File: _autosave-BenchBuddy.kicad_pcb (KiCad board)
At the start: 4 copper layers, 165.1 x 63.5 mm, 133 parts, among them K1 1461069-5, P1 24 Pin MiniFit JR, P2 CONN_3X2, P3 CONN_2, P4 12 Pin Terminal Block, P5 3 Pin TB, Q1 2N3904, Q2 DMN65D8L-7, Q3 AOD476, Q4 AOD476, SW1 Power Switch, U1 LTV-816S, U11 LM317, U2 MCP3901, U3 LMT84, U4 OPA4170, U5 MCP4801, U6 LM337T, U7 AP5726, U8 LM337T, U9 LM317

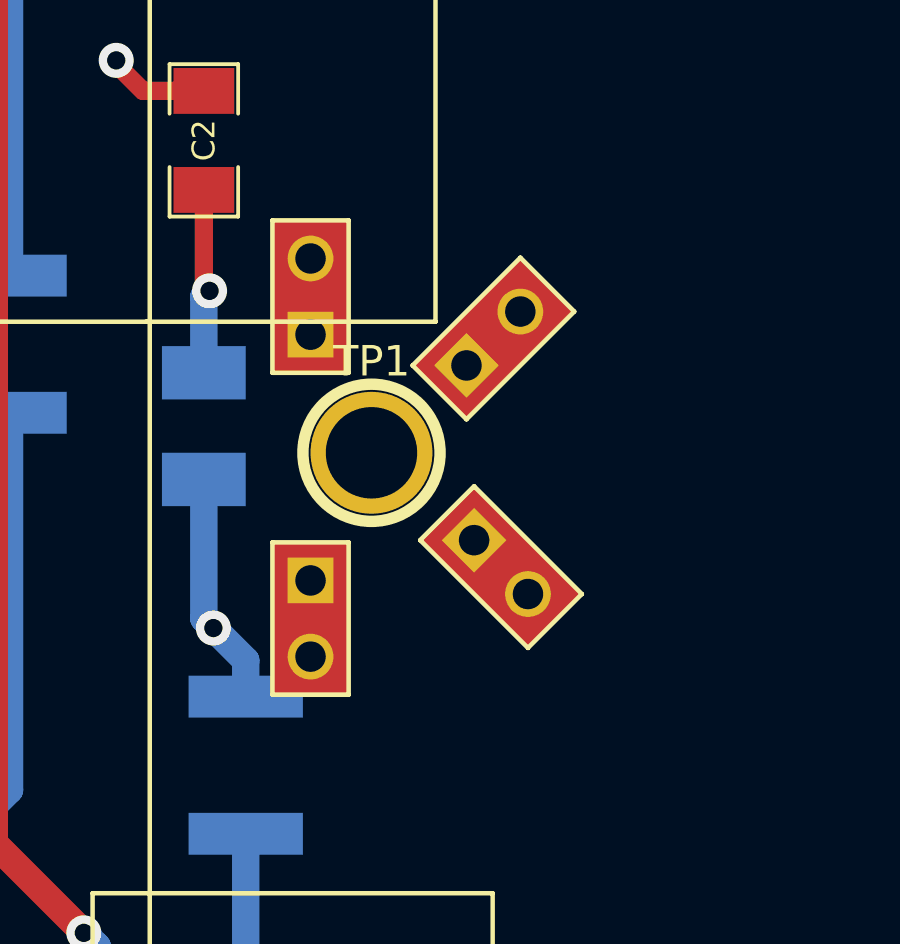
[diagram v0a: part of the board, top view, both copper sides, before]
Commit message: Connecting Grounds Together
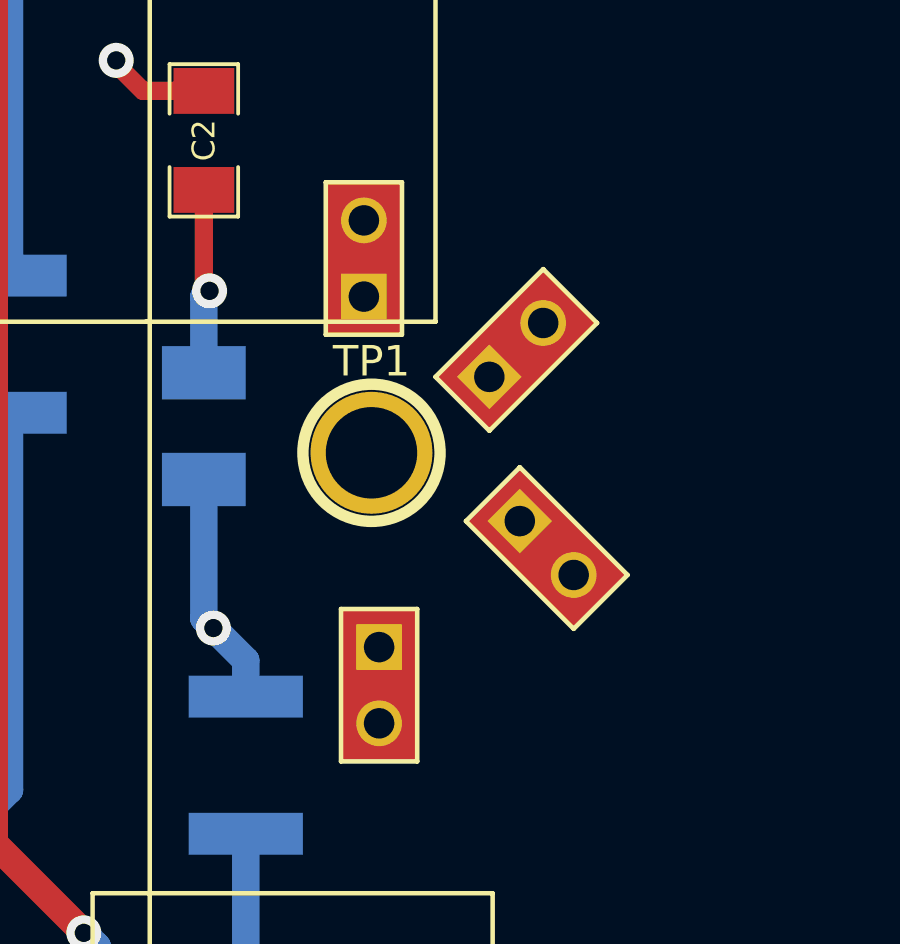
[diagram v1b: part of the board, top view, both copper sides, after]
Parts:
- moved JP4 3.19 mm to (89.9, 121.4)
- moved JP2 2.18 mm to (89.4, 107.2)
- moved JP3 1.65 mm to (95.5, 116.8)
- moved JP1 0.85 mm to (94.5, 110.2)
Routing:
- net GND: track 30.6 -> 33.9 mm
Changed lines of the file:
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@@
   (general
     (links 335)
-    (no_connects 288)
+    (no_connects 287)
     (area 45.180556 57.588999 238.38044 142.307)
     (thickness 1.6)
     (drawings 5)
-    (tracks 129)
+    (tracks 131)
     (zones 0)
     (modules 133)
@@
   )
   (module GND_POINT (layer F.Cu)
-    (at 87.63 119.1895 270)
+    (at 89.916 121.412 270)
     (descr "Connecteurs 2 pins")
     (tags "CONN DEV")
@@
   )
   (module GND_POINT (layer F.Cu)
-    (at 93.98 117.475 315)
+    (at 95.504 116.84 315)
     (descr "Connecteurs 2 pins")
     (tags "CONN DEV")
@@
   )
   (module GND_POINT (layer F.Cu)
-    (at 87.63 108.458 90)
+    (at 89.408 107.188 90)
     (descr "Connecteurs 2 pins")
     (tags "CONN DEV")
@@
   )
   (module GND_POINT (layer F.Cu)
-    (at 93.726 109.855 45)
+    (at 94.488 110.236 45)
     (descr "Connecteurs 2 pins")
     (tags "CONN DEV")
@@
   (segment (start 215.138 135.509) (end 207.3402 135.509) (width 0.9144) (layer F.Cu) (net 35))
   (segment (start 207.3402 135.509) (end 205.6384 137.2108) (width 0.9144) (layer F.Cu) (net 35))
-  (segment (start 89.662 113.665) (end 81.534 113.665) (width 1.2192) (layer GND) (net 45) (status 400000))
+  (segment (start 89.916 120.142) (end 89.916 113.919) (width 1.2192) (layer GND) (net 45) (status C00000))
+  (segment (start 89.916 113.919) (end 89.662 113.665) (width 1.2192) (layer GND) (net 45) (status C00000))
+  (segment (start 94.605974 115.941974) (end 92.964 114.3) (width 1.2192) (layer GND) (net 45) (status 400000))
+  (segment (start 90.297 114.3) (end 89.662 113.665) (width 1.2192) (layer GND) (net 45) (status C00000))
+  (segment (start 92.964 114.3) (end 90.297 114.3) (width 1.2192) (layer GND) (net 45) (status 800000))
+  (segment (start 93.589974 111.134026) (end 93.081974 111.134026) (width 1.2192) (layer GND) (net 45))
+  (segment (start 90.551 113.665) (end 89.662 113.665) (width 1.2192) (layer GND) (net 45))
+  (segment (start 93.081974 111.134026) (end 90.551 113.665) (width 1.2192) (layer GND) (net 45))
+  (segment (start 89.662 113.665) (end 81.534 113.665) (width 1.2192) (layer GND) (net 45))
   (segment (start 81.534 113.665) (end 81.407 113.792) (width 1.2192) (layer GND) (net 45))
-  (segment (start 93.081974 116.576974) (end 92.573974 116.576974) (width 0.9144) (layer GND) (net 45))
-  (segment (start 92.573974 116.576974) (end 89.662 113.665) (width 0.9144) (layer GND) (net 45))
   (segment (start 87.63 109.728) (end 87.63 111.633) (width 0.9144) (layer GND) (net 45))
   (segment (start 87.63 111.633) (end 89.662 113.665) (width 0.9144) (layer GND) (net 45))
@@
   (segment (start 81.153 100.711) (end 81.153 100.584) (width 0.6096) (layer F.Cu) (net 45))
   (segment (start 82.042 101.6) (end 81.153 100.711) (width 0.6096) (layer F.Cu) (net 45))
-  (segment (start 92.827974 110.753026) (end 92.573974 110.753026) (width 0.9144) (layer GND) (net 45))
-  (segment (start 92.573974 110.753026) (end 89.662 113.665) (width 0.9144) (layer GND) (net 45))
-  (segment (start 87.63 117.9195) (end 87.63 115.697) (width 0.9144) (layer GND) (net 45))
-  (segment (start 87.63 115.697) (end 89.662 113.665) (width 0.9144) (layer GND) (net 45))
   (segment (start 171.958 119.9007) (end 171.958 118.542) (width 0.6096) (layer B.Cu) (net 46))
   (via (at 173 117.5) (size 1.1684) (drill 0.6096) (layers F.Cu B.Cu) (net 46))
@@
   (segment (start 83.2485 137.16) (end 65.9765 137.16) (width 0.9144) (layer B.Cu) (net 51))
   (segment (start 85.471 134.9375) (end 83.2485 137.16) (width 0.9144) (layer B.Cu) (net 51))
-  (zone (net 46) (net_name GND_LED) (layer GND) (hatch edge 0.508)
-    (connect_pads (clearance 0.508))
-    (min_thickness 0.254)
-    (fill (arc_segments 16) (thermal_gap 0.508) (thermal_bridge_width 0.508))
-    (polygon
-      (pts
-        (xy 90.551 114.046) (xy 90.551 123.063) (xy 179.0065 123.444) (xy 179.0065 119.507) (xy 217.9955 119.507)
-        (xy 217.932 113.9825) (xy 90.6145 113.9825)
-      )
-    )
-  )
-  (zone (net 42) (net_name AGND) (layer GND) (hatch edge 0.508)
-    (connect_pads (clearance 0.508))
-    (min_thickness 0.254)
-    (fill (arc_segments 16) (thermal_gap 0.508) (thermal_bridge_width 0.508))
-    (polygon
-      (pts
-        (xy 89.5985 112.9665) (xy 89.5985 92.837) (xy 184.404 93.091) (xy 184.404 84.963) (xy 209.7405 84.963)
-        (xy 209.7405 95.758) (xy 218.2495 95.631) (xy 218.1225 112.776) (xy 89.5985 113.03)
-      )
-    )
-  )
   (zone (net 47) (net_name GND_PWR) (layer GND) (hatch edge 0.508)
     (connect_pads (clearance 0.508))
@@
     (polygon
       (pts
-        (xy 88.7095 113.0935) (xy 88.7095 92.075) (xy 183.261 91.948) (xy 183.3245 84.1375) (xy 210.7565 83.8835)
-        (xy 210.693 94.615) (xy 218.1225 94.5515) (xy 218.186 77.2795) (xy 86.487 77.47) (xy 86.5505 113.03)
-        (xy 88.5825 113.0935)
+        (xy 218.186 77.2795) (xy 218.1225 94.5515) (xy 210.693 94.615) (xy 210.7565 83.8835) (xy 183.3245 84.1375)
+        (xy 183.261 91.948) (xy 92.456 92.069967) (xy 92.456 107.696) (xy 88.7095 107.696) (xy 88.7095 113.0935)
+        (xy 88.5825 113.0935) (xy 86.5505 113.03) (xy 86.540975 107.696) (xy 86.36 107.696) (xy 86.36 77.724)
+        (xy 86.487453 77.724) (xy 86.487 77.47) (xy 218.186 77.2795)
       )
     )
@@
     (polygon
       (pts
-        (xy 197.358 140.3985) (xy 88.7095 140.208) (xy 86.5505 140.208) (xy 86.614 113.9825) (xy 88.7095 113.9825)
-        (xy 88.646 124.5235) (xy 196.977 124.46) (xy 196.977 128.524) (xy 187.96 128.524) (xy 188.0235 135.001)
-        (xy 197.358 135.001)
+        (xy 197.358 140.3985) (xy 88.7095 140.208) (xy 86.5505 140.208) (xy 86.595963 121.431526) (xy 86.36 118.364)
+        (xy 86.603391 118.364) (xy 86.614 113.9825) (xy 88.7095 113.9825) (xy 88.683105 118.364) (xy 92.456 118.364)
+        (xy 92.456 124.521266) (xy 196.977 124.46) (xy 196.977 128.524) (xy 187.96 128.524) (xy 188.0235 135.001)
+        (xy 197.358 135.001) (xy 197.358 140.3985)
+      )
+    )
+  )
+  (zone (net 42) (net_name AGND) (layer GND) (hatch edge 0.508)
+    (connect_pads (clearance 0.508))
+    (min_thickness 0.254)
+    (fill (arc_segments 16) (thermal_gap 0.508) (thermal_bridge_width 0.508))
+    (polygon
+      (pts
+        (xy 217.932 113.284) (xy 92.964 113.284) (xy 92.964 92.964) (xy 97.028 92.964) (xy 184.404 92.456)
+        (xy 184.404 84.836) (xy 209.804 84.836) (xy 209.804 95.504) (xy 217.932 95.504)
+      )
+    )
+  )
+  (zone (net 46) (net_name GND_LED) (layer GND) (hatch edge 0.508)
+    (connect_pads (clearance 0.508))
+    (min_thickness 0.254)
+    (fill (arc_segments 16) (thermal_gap 0.508) (thermal_bridge_width 0.508))
+    (polygon
+      (pts
+        (xy 92.964 114.3) (xy 92.964 123.952) (xy 189.992 123.952) (xy 189.992 120.396) (xy 218.44 120.904)
+        (xy 218.44 113.792) (xy 92.964 114.3)
       )
     )
